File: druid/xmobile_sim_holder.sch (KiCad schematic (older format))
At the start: 40 parts

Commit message: Add xmega pcb, Add SIM800 pcb Add SRAM pcb, Start to draw sim card holder pcb
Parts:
- U?: footprint (none) -> druid:SIM800C
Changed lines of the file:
@@
 F 0 "U?" H 6675 4500 60  0000 C CNN
 F 1 "SIM800C" H 5975 4500 60  0000 C CNN
-F 2 "" H 6625 3525 60  0000 C CNN
+F 2 "druid:SIM800C" H 6625 3525 60  0000 C CNN
 F 3 "" H 6625 3525 60  0000 C CNN
 	1    6625 3525

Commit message: SIM cart holder completed. Add micro B slot added
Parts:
- P?: footprint (none) -> Connectors_USB:USB_Micro-B_Molex_47346-0001
- U?: footprint (none) -> druid:molex-microSIM_SD-78646-001
- U?: footprint MODULE -> druid:TSOP-6_CASE-318G-02
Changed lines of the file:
@@
 F 0 "U?" H 6675 4500 60  0000 C CNN
 F 1 "SIM800C" H 5975 4500 60  0000 C CNN
-F 2 "druid:SIM800C" H 6625 3525 60  0000 C CNN
+F 2 "druid:SIM800C" H 6500 3475 60  0000 C CNN
 F 3 "" H 6625 3525 60  0000 C CNN
 	1    6625 3525
@@
 F 0 "U?" H 4875 5575 60  0000 C CNN
 F 1 "78646-3001" H 4925 5725 60  0000 C CNN
-F 2 "" H 4775 5825 60  0000 C CNN
+F 2 "druid:molex-microSIM_SD-78646-001" H 4850 5400 60  0000 C CNN
 F 3 "" H 4775 5825 60  0000 C CNN
 	1    4775 5775
@@
 F 0 "D?" H 3350 6875 60  0000 C CNN
 F 1 "SMF05C" H 3075 6875 60  0000 C CNN
-F 2 "semtech:SOT363" H 3240 6650 60  0000 C CNN
+F 2 "semtech:SOT363" H 3250 6975 60  0000 C CNN
 F 3 "" H 3240 6650 60  0000 C CNN
 	1    3250 6650
@@
 F 0 "U?" H 8625 1750 50  0000 C CNN
 F 1 "STF202-22T1G" H 8625 1950 50  0000 C CNN
-F 2 "MODULE" H 8625 1850 50  0001 C CNN
+F 2 "druid:TSOP-6_CASE-318G-02" H 8600 1500 50  0000 C CNN
 F 3 "DOCUMENTATION" H 8625 1850 50  0001 C CNN
 	1    8625 1850
@@
 F 0 "P?" H 10125 1750 50  0000 C CNN
 F 1 "USB_A" H 9875 2150 50  0000 C CNN
-F 2 "" V 9875 1850 50  0000 C CNN
+F 2 "Connectors_USB:USB_Micro-B_Molex_47346-0001" V 9875 1850 50  0000 C CNN
 F 3 "" V 9875 1850 50  0000 C CNN
 	1    9925 1950

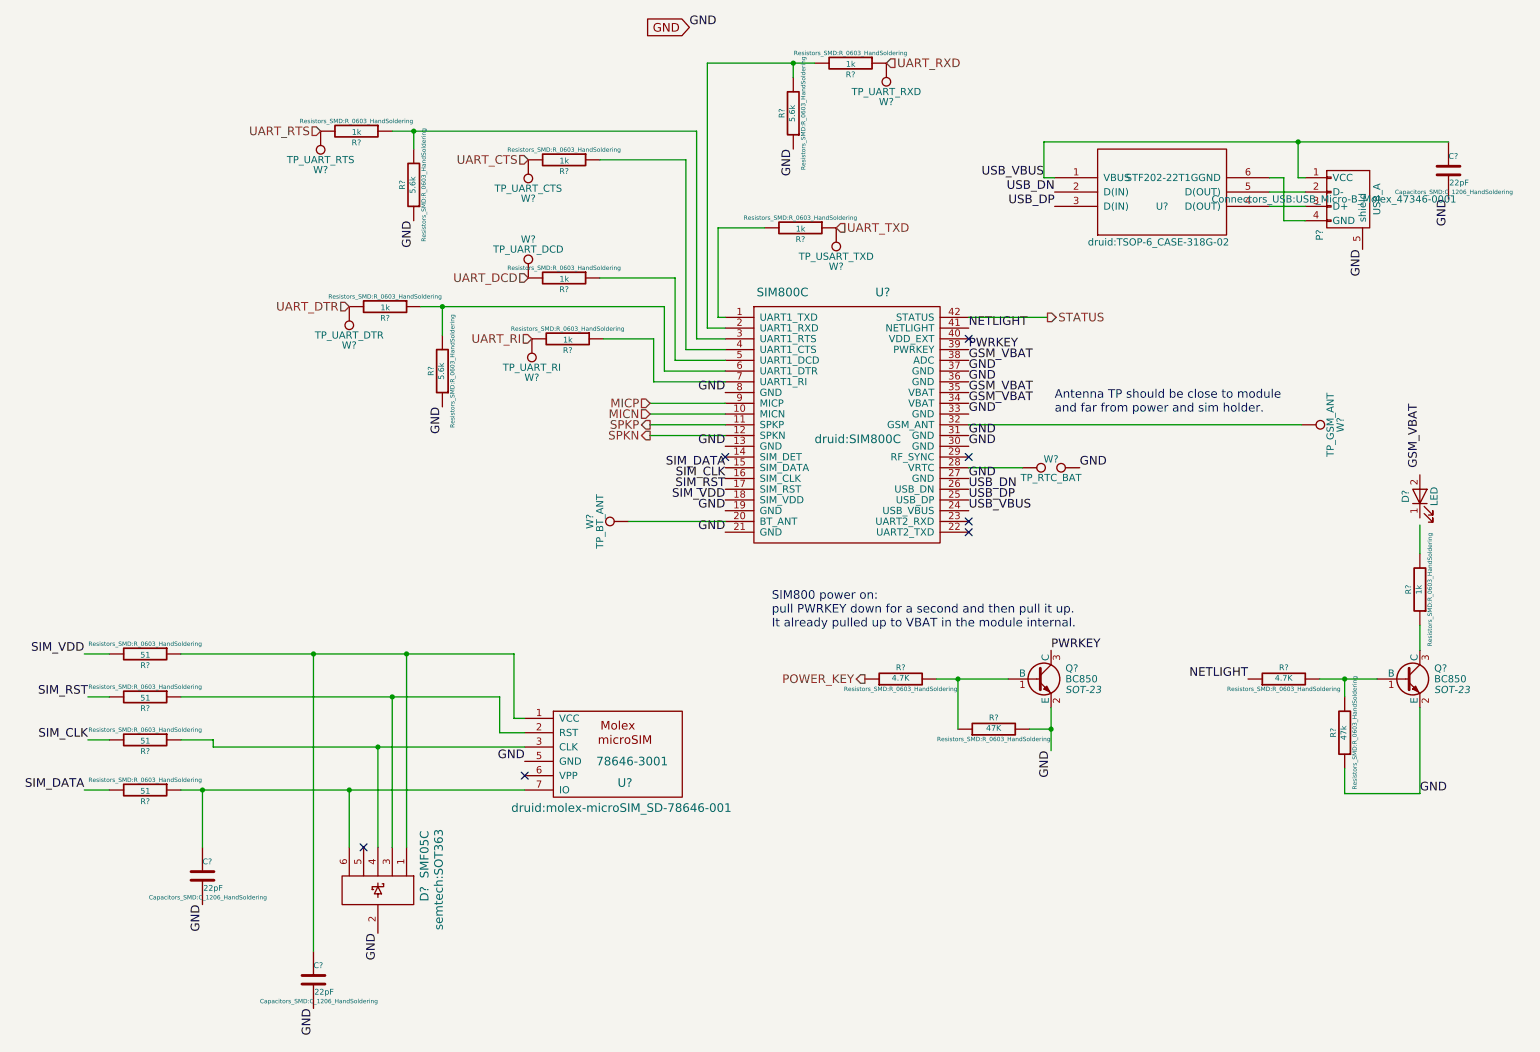
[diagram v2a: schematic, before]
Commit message: Old buttons replaced by membran buttons (electic and pcb) Added pcb for MAX7370 Cleared PCBs of resistor, capacitors and diodes
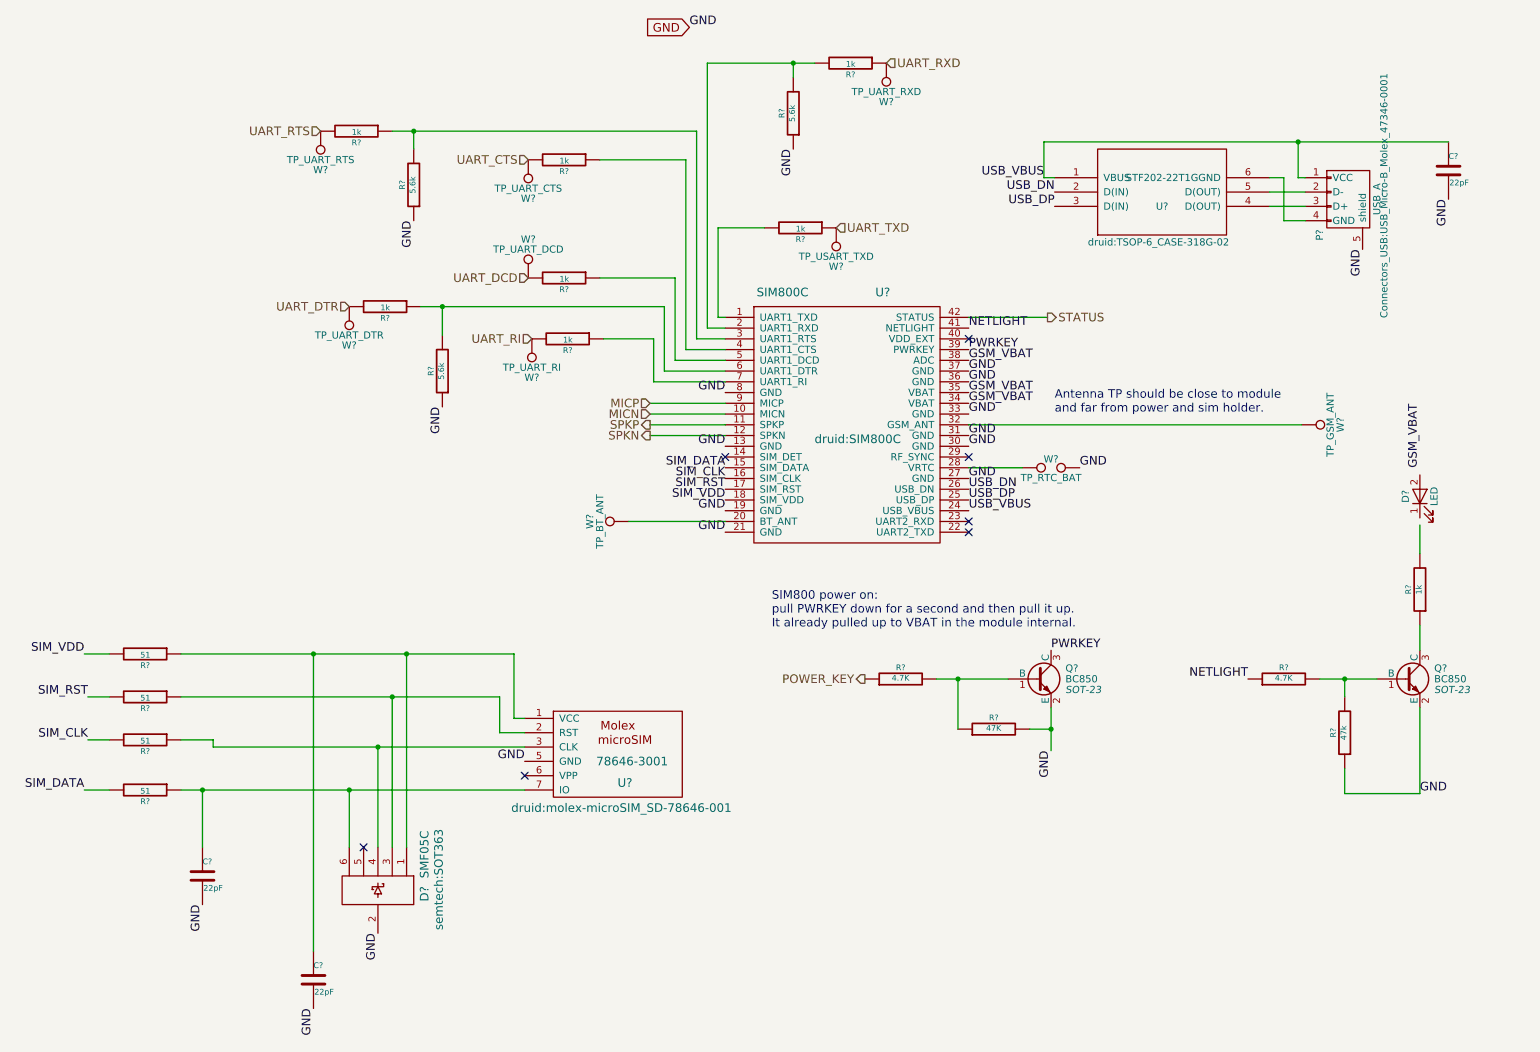
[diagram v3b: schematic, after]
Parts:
- C? (x3): footprint Capacitors_SMD:C_1206_HandSoldering -> (none)
- R? (x19): footprint Resistors_SMD:R_0603_HandSoldering -> (none)
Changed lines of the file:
@@
 F 0 "R?" V 1605 6025 40  0000 C CNN
 F 1 "51" V 1532 6026 40  0000 C CNN
-F 2 "Resistors_SMD:R_0603_HandSoldering" V 1455 6025 30  0000 C CNN
+F 2 "" V 1455 6025 30  0000 C CNN
 F 3 "" H 1525 6025 30  0000 C CNN
 	1    1525 6025
@@
 F 0 "C?" H 1925 6725 40  0000 L CNN
 F 1 "22pF" H 1931 6540 40  0000 L CNN
-F 2 "Capacitors_SMD:C_1206_HandSoldering" H 1963 6475 30  0000 C CNN
+F 2 "" H 1963 6475 30  0000 C CNN
 F 3 "" H 1925 6625 60  0000 C CNN
 	1    1925 6625
@@
 F 0 "R?" V 1605 5675 40  0000 C CNN
 F 1 "51" V 1532 5676 40  0000 C CNN
-F 2 "Resistors_SMD:R_0603_HandSoldering" V 1455 5675 30  0000 C CNN
+F 2 "" V 1455 5675 30  0000 C CNN
 F 3 "" H 1525 5675 30  0000 C CNN
 	1    1525 5675
@@
 F 0 "R?" V 1605 5375 40  0000 C CNN
 F 1 "51" V 1532 5376 40  0000 C CNN
-F 2 "Resistors_SMD:R_0603_HandSoldering" V 1455 5375 30  0000 C CNN
+F 2 "" V 1455 5375 30  0000 C CNN
 F 3 "" H 1525 5375 30  0000 C CNN
 	1    1525 5375
@@
 F 0 "R?" V 1605 5075 40  0000 C CNN
 F 1 "51" V 1532 5076 40  0000 C CNN
-F 2 "Resistors_SMD:R_0603_HandSoldering" V 1455 5075 30  0000 C CNN
+F 2 "" V 1455 5075 30  0000 C CNN
 F 3 "" H 1525 5075 30  0000 C CNN
 	1    1525 5075
@@
 F 0 "C?" H 2700 7450 40  0000 L CNN
 F 1 "22pF" H 2706 7265 40  0000 L CNN
-F 2 "Capacitors_SMD:C_1206_HandSoldering" H 2738 7200 30  0000 C CNN
+F 2 "" H 2738 7200 30  0000 C CNN
 F 3 "" H 2700 7350 60  0000 C CNN
 	1    2700 7350
@@
 F 0 "R?" V 10505 4625 40  0000 C CNN
 F 1 "1k" V 10432 4626 40  0000 C CNN
-F 2 "Resistors_SMD:R_0603_HandSoldering" V 10355 4625 30  0000 C CNN
+F 2 "" V 10355 4625 30  0000 C CNN
 F 3 "" H 10425 4625 30  0000 C CNN
 	1    10425 4625
@@
 F 0 "R?" V 9980 5625 40  0000 C CNN
 F 1 "47k" V 9907 5626 40  0000 C CNN
-F 2 "Resistors_SMD:R_0603_HandSoldering" V 9830 5625 30  0000 C CNN
+F 2 "" V 9830 5625 30  0000 C CNN
 F 3 "" H 9900 5625 30  0000 C CNN
 	1    9900 5625
@@
 F 0 "R?" V 9555 5250 40  0000 C CNN
 F 1 "4.7K" V 9482 5251 40  0000 C CNN
-F 2 "Resistors_SMD:R_0603_HandSoldering" V 9405 5250 30  0000 C CNN
+F 2 "" V 9405 5250 30  0000 C CNN
 F 3 "" H 9475 5250 30  0000 C CNN
 	1    9475 5250
@@
 F 0 "R?" V 6880 5250 40  0000 C CNN
 F 1 "4.7K" V 6807 5251 40  0000 C CNN
-F 2 "Resistors_SMD:R_0603_HandSoldering" V 6730 5250 30  0000 C CNN
+F 2 "" V 6730 5250 30  0000 C CNN
 F 3 "" H 6800 5250 30  0000 C CNN
 	1    6800 5250
@@
 F 0 "R?" V 7530 5600 40  0000 C CNN
 F 1 "47K" V 7457 5601 40  0000 C CNN
-F 2 "Resistors_SMD:R_0603_HandSoldering" V 7380 5600 30  0000 C CNN
+F 2 "" V 7380 5600 30  0000 C CNN
 F 3 "" H 7450 5600 30  0000 C CNN
 	1    7450 5600
@@
 F 0 "R?" V 4555 2875 40  0000 C CNN
 F 1 "1k" V 4482 2876 40  0000 C CNN
-F 2 "Resistors_SMD:R_0603_HandSoldering" V 4405 2875 30  0000 C CNN
+F 2 "" V 4405 2875 30  0000 C CNN
 F 3 "" H 4475 2875 30  0000 C CNN
 	1    4475 2875
@@
 F 0 "R?" V 3280 2650 40  0000 C CNN
 F 1 "1k" V 3207 2651 40  0000 C CNN
-F 2 "Resistors_SMD:R_0603_HandSoldering" V 3130 2650 30  0000 C CNN
+F 2 "" V 3130 2650 30  0000 C CNN
 F 3 "" H 3200 2650 30  0000 C CNN
 	1    3200 2650
@@
 F 0 "R?" V 3680 3100 40  0000 C CNN
 F 1 "5.6k" V 3607 3101 40  0000 C CNN
-F 2 "Resistors_SMD:R_0603_HandSoldering" V 3530 3100 30  0000 C CNN
+F 2 "" V 3530 3100 30  0000 C CNN
 F 3 "" H 3600 3100 30  0000 C CNN
 	1    3600 3100
@@
 F 0 "R?" V 4530 2450 40  0000 C CNN
 F 1 "1k" V 4457 2451 40  0000 C CNN
-F 2 "Resistors_SMD:R_0603_HandSoldering" V 4380 2450 30  0000 C CNN
+F 2 "" V 4380 2450 30  0000 C CNN
 F 3 "" H 4450 2450 30  0000 C CNN
 	1    4450 2450
@@
 F 0 "R?" V 4530 1625 40  0000 C CNN
 F 1 "1k" V 4457 1626 40  0000 C CNN
-F 2 "Resistors_SMD:R_0603_HandSoldering" V 4380 1625 30  0000 C CNN
+F 2 "" V 4380 1625 30  0000 C CNN
 F 3 "" H 4450 1625 30  0000 C CNN
 	1    4450 1625
@@
 F 0 "R?" V 3080 1425 40  0000 C CNN
 F 1 "1k" V 3007 1426 40  0000 C CNN
-F 2 "Resistors_SMD:R_0603_HandSoldering" V 2930 1425 30  0000 C CNN
+F 2 "" V 2930 1425 30  0000 C CNN
 F 3 "" H 3000 1425 30  0000 C CNN
 	1    3000 1425
@@
 F 0 "R?" V 3480 1800 40  0000 C CNN
 F 1 "5.6k" V 3407 1801 40  0000 C CNN
-F 2 "Resistors_SMD:R_0603_HandSoldering" V 3330 1800 30  0000 C CNN
+F 2 "" V 3330 1800 30  0000 C CNN
 F 3 "" H 3400 1800 30  0000 C CNN
 	1    3400 1800
@@
 F 0 "R?" V 6530 950 40  0000 C CNN
 F 1 "1k" V 6457 951 40  0000 C CNN
-F 2 "Resistors_SMD:R_0603_HandSoldering" V 6380 950 30  0000 C CNN
+F 2 "" V 6380 950 30  0000 C CNN
 F 3 "" H 6450 950 30  0000 C CNN
 	1    6450 950
@@
 F 0 "R?" V 6130 1300 40  0000 C CNN
 F 1 "5.6k" V 6057 1301 40  0000 C CNN
-F 2 "Resistors_SMD:R_0603_HandSoldering" V 5980 1300 30  0000 C CNN
+F 2 "" V 5980 1300 30  0000 C CNN
 F 3 "" H 6050 1300 30  0000 C CNN
 	1    6050 1300
@@
 F 0 "R?" V 6180 2100 40  0000 C CNN
 F 1 "1k" V 6107 2101 40  0000 C CNN
-F 2 "Resistors_SMD:R_0603_HandSoldering" V 6030 2100 30  0000 C CNN
+F 2 "" V 6030 2100 30  0000 C CNN
 F 3 "" H 6100 2100 30  0000 C CNN
 	1    6100 2100
@@
 F 0 "P?" H 10125 1750 50  0000 C CNN
 F 1 "USB_A" H 9875 2150 50  0000 C CNN
-F 2 "Connectors_USB:USB_Micro-B_Molex_47346-0001" V 9875 1850 50  0000 C CNN
+F 2 "Connectors_USB:USB_Micro-B_Molex_47346-0001" H 9850 2200 50  0000 C CNN
 F 3 "" V 9875 1850 50  0000 C CNN
 	1    9925 1950
@@
 F 0 "C?" H 10625 1800 40  0000 L CNN
 F 1 "22pF" H 10631 1615 40  0000 L CNN
-F 2 "Capacitors_SMD:C_1206_HandSoldering" H 10663 1550 30  0000 C CNN
+F 2 "" H 10663 1550 30  0000 C CNN
 F 3 "" H 10625 1700 60  0000 C CNN
 	1    10625 1700

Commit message: Change PDI connector.
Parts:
- C? (x3): value 22pF -> 22p
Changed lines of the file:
@@
 P 1925 6625
 F 0 "C?" H 1925 6725 40  0000 L CNN
-F 1 "22pF" H 1931 6540 40  0000 L CNN
+F 1 "22p" H 1931 6540 40  0000 L CNN
 F 2 "" H 1963 6475 30  0000 C CNN
 F 3 "" H 1925 6625 60  0000 C CNN
@@
 P 2700 7350
 F 0 "C?" H 2700 7450 40  0000 L CNN
-F 1 "22pF" H 2706 7265 40  0000 L CNN
+F 1 "22p" H 2706 7265 40  0000 L CNN
 F 2 "" H 2738 7200 30  0000 C CNN
 F 3 "" H 2700 7350 60  0000 C CNN
@@
 P 10625 1700
 F 0 "C?" H 10625 1800 40  0000 L CNN
-F 1 "22pF" H 10631 1615 40  0000 L CNN
+F 1 "22p" H 10631 1615 40  0000 L CNN
 F 2 "" H 10663 1550 30  0000 C CNN
 F 3 "" H 10625 1700 60  0000 C CNN

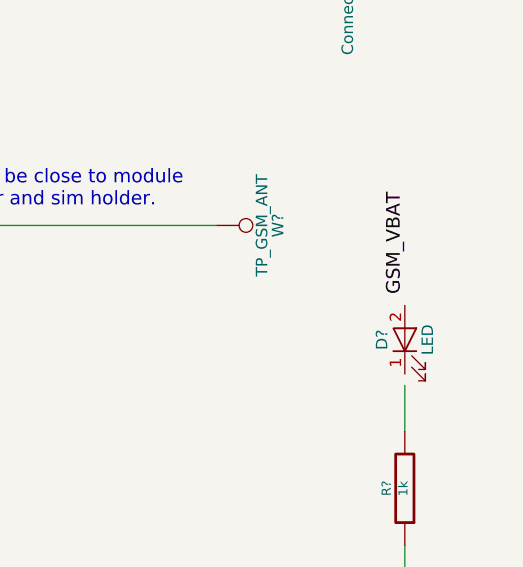
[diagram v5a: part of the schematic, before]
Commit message: Add some packages
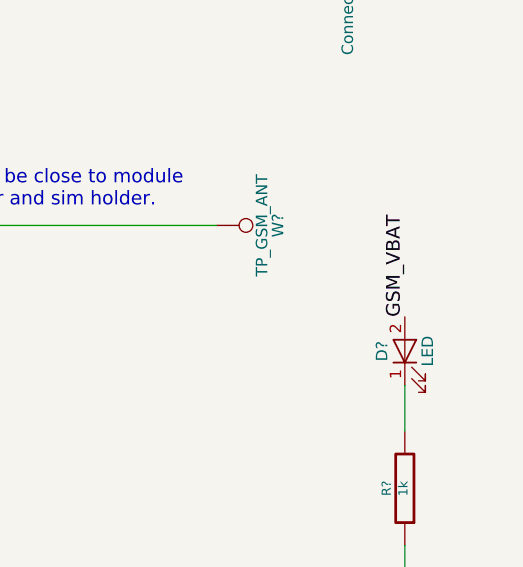
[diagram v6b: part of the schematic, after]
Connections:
- net GSM_VBAT: now also D?.2 (A)
- net at D?.1 (K): now also R?.2
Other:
- moved on the sheet: D?
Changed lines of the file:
@@
 Text Label 7275 3250 0    60   ~ 0
 GSM_VBAT
-Text Label 10425 3775 1    60   ~ 0
+Text Label 10425 3875 1    60   ~ 0
 GSM_VBAT
 $Comp
 L LED-RESCUE-xmobile D?
 U 1 1 5C46F9F6
-P 10425 3975
-F 0 "D?" H 10425 4075 50  0000 C CNN
-F 1 "LED" H 10425 3875 50  0000 C CNN
-F 2 "" H 10425 3975 50  0000 C CNN
-F 3 "" H 10425 3975 50  0000 C CNN
-	1    10425 3975
+P 10425 4025
+F 0 "D?" H 10425 4125 50  0000 C CNN
+F 1 "LED" H 10425 3925 50  0000 C CNN
+F 2 "" H 10425 4025 50  0000 C CNN
+F 3 "" H 10425 4025 50  0000 C CNN
+	1    10425 4025
 	0    -1   -1   0
 $EndComp
@@
 Wire Wire Line
 	7275 3775 7650 3775
-Text Label 8050 3775 0    60   ~ 0
-GND
 $Comp
 L TEST_1P W?
@@
 Wire Wire Line
 	5575 3550 5050 3550
+Text Label 8050 3775 0    60   ~ 0
+GND
 $EndSCHEMATC

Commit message: move to kicad 5
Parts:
- C? (x3): symbol C-RESCUE-xmobile -> xmobile-rescue:C-RESCUE-xmobile
- D?: symbol SMF05C -> xmobile-rescue:SMF05C
- D?: symbol LED-RESCUE-xmobile -> xmobile-rescue:LED-RESCUE-xmobile
- P?: symbol USB_A-RESCUE-xmobile -> xmobile-rescue:USB_A-RESCUE-xmobile
- Q? (x2): symbol BC850 -> xmobile-rescue:BC850
- R? (x19): symbol R-RESCUE-xmobile -> xmobile-rescue:R-RESCUE-xmobile
- U?: symbol SIM800C -> xmobile-rescue:SIM800C
- U?: symbol 78646-3001 -> xmobile-rescue:78646-3001
- U?: symbol STF202-22T1G -> xmobile-rescue:STF202-22T1G
- W?: symbol TEST-RESCUE-xmobile -> xmobile-rescue:TEST-RESCUE-xmobile
- W? (x9): symbol TEST_1P -> xmobile-rescue:TEST_1P
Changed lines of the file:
@@
-EESchema Schematic File Version 2
-LIBS:xmobile-rescue
-LIBS:power
-LIBS:device
-LIBS:transistors
-LIBS:conn
-LIBS:linear
-LIBS:regul
-LIBS:74xx
-LIBS:cmos4000
-LIBS:adc-dac
-LIBS:memory
-LIBS:xilinx
-LIBS:microcontrollers
-LIBS:dsp
-LIBS:microchip
-LIBS:analog_switches
-LIBS:motorola
-LIBS:texas
-LIBS:intel
-LIBS:audio
-LIBS:interface
-LIBS:digital-audio
-LIBS:philips
-LIBS:display
-LIBS:cypress
-LIBS:siliconi
-LIBS:opto
-LIBS:atmel
-LIBS:contrib
-LIBS:valves
-LIBS:XC6206P332MR
-LIBS:STF202-22T1G
-LIBS:MCP73871
-LIBS:switch1
-LIBS:SRAM
-LIBS:xmega128a1u_bga100
-LIBS:sim-holders
-LIBS:max7370
-LIBS:tp4056
+EESchema Schematic File Version 4
 LIBS:xmobile-cache
-EELAYER 25 0
+EELAYER 26 0
 EELAYER END
 $Descr A4 11693 8268
@@
 GND
 $Comp
-L SIM800C U?
+L xmobile-rescue:SIM800C U?
 U 1 1 5C46A8F4
 P 6625 3525
@@
 $EndComp
 $Comp
-L 78646-3001 U?
+L xmobile-rescue:78646-3001 U?
 U 1 1 5C46ADE6
 P 4775 5775
@@
 SIM_DATA
 $Comp
-L SMF05C D?
+L xmobile-rescue:SMF05C D?
 U 1 1 5C46C4AB
 P 3250 6650
@@
 $EndComp
 $Comp
-L R-RESCUE-xmobile R?
+L xmobile-rescue:R-RESCUE-xmobile R?
 U 1 1 5C46C6D5
 P 1525 6025
@@
 Connection ~ 2950 6025
 $Comp
-L C-RESCUE-xmobile C?
+L xmobile-rescue:C-RESCUE-xmobile C?
 U 1 1 5C46CACB
 P 1925 6625
@@
 Connection ~ 1925 6025
 $Comp
-L R-RESCUE-xmobile R?
+L xmobile-rescue:R-RESCUE-xmobile R?
 U 1 1 5C46D160
 P 1525 5675
@@
 $EndComp
 $Comp
-L R-RESCUE-xmobile R?
+L xmobile-rescue:R-RESCUE-xmobile R?
 U 1 1 5C46D2D8
 P 1525 5375
@@
 $EndComp
 $Comp
-L R-RESCUE-xmobile R?
+L xmobile-rescue:R-RESCUE-xmobile R?
 U 1 1 5C46D4E7
 P 1525 5075
@@
 GND
 $Comp
-L C-RESCUE-xmobile C?
+L xmobile-rescue:C-RESCUE-xmobile C?
 U 1 1 5C46E5BE
 P 2700 7350
@@
 GND
 $Comp
-L BC850 Q?
+L xmobile-rescue:BC850 Q?
 U 1 1 5C46E88A
 P 10325 5250
@@
 GSM_VBAT
 $Comp
-L LED-RESCUE-xmobile D?
+L xmobile-rescue:LED-RESCUE-xmobile D?
 U 1 1 5C46F9F6
 P 10425 4025
@@
 $EndComp
 $Comp
-L R-RESCUE-xmobile R?
+L xmobile-rescue:R-RESCUE-xmobile R?
 U 1 1 5C46FC7D
 P 10425 4625
@@
 $EndComp
 $Comp
-L R-RESCUE-xmobile R?
+L xmobile-rescue:R-RESCUE-xmobile R?
 U 1 1 5C4702F9
 P 9900 5625
@@
 	10425 4175 10425 4375
 $Comp
-L R-RESCUE-xmobile R?
+L xmobile-rescue:R-RESCUE-xmobile R?
 U 1 1 5C470F26
 P 9475 5250
@@
 NETLIGHT
 $Comp
-L BC850 Q?
+L xmobile-rescue:BC850 Q?
 U 1 1 5C473781
 P 7750 5250
@@
 $EndComp
 $Comp
-L R-RESCUE-xmobile R?
+L xmobile-rescue:R-RESCUE-xmobile R?
 U 1 1 5C4739DE
 P 6800 5250
@@
 $EndComp
 $Comp
-L R-RESCUE-xmobile R?
+L xmobile-rescue:R-RESCUE-xmobile R?
 U 1 1 5C473BE2
 P 7450 5600
@@
 GND
 $Comp
-L R-RESCUE-xmobile R?
+L xmobile-rescue:R-RESCUE-xmobile R?
 U 1 1 5C47BC42
 P 4475 2875
@@
 	5075 3175 5575 3175
 $Comp
-L R-RESCUE-xmobile R?
+L xmobile-rescue:R-RESCUE-xmobile R?
 U 1 1 5C47CD2E
 P 3200 2650
@@
 Connection ~ 3600 2650
 $Comp
-L R-RESCUE-xmobile R?
+L xmobile-rescue:R-RESCUE-xmobile R?
 U 1 1 5C47D122
 P 3600 3100
@@
 $EndComp
 $Comp
-L R-RESCUE-xmobile R?
+L xmobile-rescue:R-RESCUE-xmobile R?
 U 1 1 5C47D858
 P 4450 2450
@@
 	5225 3025 5575 3025
 $Comp
-L R-RESCUE-xmobile R?
+L xmobile-rescue:R-RESCUE-xmobile R?
 U 1 1 5C47DF7C
 P 4450 1625
@@
 	5300 1625 4700 1625
 $Comp
-L R-RESCUE-xmobile R?
+L xmobile-rescue:R-RESCUE-xmobile R?
 U 1 1 5C47E9C4
 P 3000 1425
@@
 $EndComp
 $Comp
-L R-RESCUE-xmobile R?
+L xmobile-rescue:R-RESCUE-xmobile R?
 U 1 1 5C47EDF5
 P 3400 1800
@@
 Connection ~ 3400 1425
 $Comp
-L R-RESCUE-xmobile R?
+L xmobile-rescue:R-RESCUE-xmobile R?
 U 1 1 5C47FAB8
 P 6450 950
@@
 $EndComp
 $Comp
-L R-RESCUE-xmobile R?
+L xmobile-rescue:R-RESCUE-xmobile R?
 U 1 1 5C47FCB5
 P 6050 1300
@@
 GND
 $Comp
-L TEST-RESCUE-xmobile W?
+L xmobile-rescue:TEST-RESCUE-xmobile W?
 U 1 1 5C481A0A
 P 7850 3775
@@
 	7275 3775 7650 3775
 $Comp
-L TEST_1P W?
+L xmobile-rescue:TEST_1P W?
 U 1 1 5C481C47
 P 9600 3475
@@
 NoConn ~ 7275 2875
 $Comp
-L TEST_1P W?
+L xmobile-rescue:TEST_1P W?
 U 1 1 5C483444
 P 4900 4150
@@
 NoConn ~ 5575 3700
 $Comp
-L R-RESCUE-xmobile R?
+L xmobile-rescue:R-RESCUE-xmobile R?
 U 1 1 5C48469B
 P 6100 2100
@@
 GND
 $Comp
-L TEST_1P W?
+L xmobile-rescue:TEST_1P W?
 U 1 1 5C490798
 P 6700 950
@@
 $EndComp
 $Comp
-L TEST_1P W?
+L xmobile-rescue:TEST_1P W?
 U 1 1 5C491932
 P 2750 1425
@@
 $EndComp
 $Comp
-L TEST_1P W?
+L xmobile-rescue:TEST_1P W?
 U 1 1 5C491C83
 P 2950 2650
@@
 $EndComp
 $Comp
-L TEST_1P W?
+L xmobile-rescue:TEST_1P W?
 U 1 1 5C4925FE
 P 4200 1625
@@
 $EndComp
 $Comp
-L TEST_1P W?
+L xmobile-rescue:TEST_1P W?
 U 1 1 5C49272C
 P 4200 2450
@@
 $EndComp
 $Comp
-L TEST_1P W?
+L xmobile-rescue:TEST_1P W?
 U 1 1 5C4928AD
 P 4225 2875
@@
 $EndComp
 $Comp
-L TEST_1P W?
+L xmobile-rescue:TEST_1P W?
 U 1 1 5C492A5F
 P 6350 2100
@@
 $EndComp
 $Comp
-L STF202-22T1G U?
+L xmobile-rescue:STF202-22T1G U?
 U 1 1 5C497719
 P 8625 1850
@@
 $EndComp
 $Comp
-L USB_A-RESCUE-xmobile P?
+L xmobile-rescue:USB_A-RESCUE-xmobile P?
 U 1 1 5C499B15
 P 9925 1950
@@
 	7800 1750 7875 1750
 $Comp
-L C-RESCUE-xmobile C?
+L xmobile-rescue:C-RESCUE-xmobile C?
 U 1 1 5C49B02E
 P 10625 1700
